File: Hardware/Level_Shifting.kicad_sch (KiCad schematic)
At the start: 49 parts, among them J11 SMA_Edge, J12 SMA_Edge, SW4 SPDT_Slide_SMD_7.2x3.5mm, U10 74LVC2T45DC, U12 74LVC2T45DC, U14 74LVC2T45DC, U15 74LVC2T45DC, U16 74LVC2T45DC, U8 74LVC2T45DC, U9 74LVC2T45DC

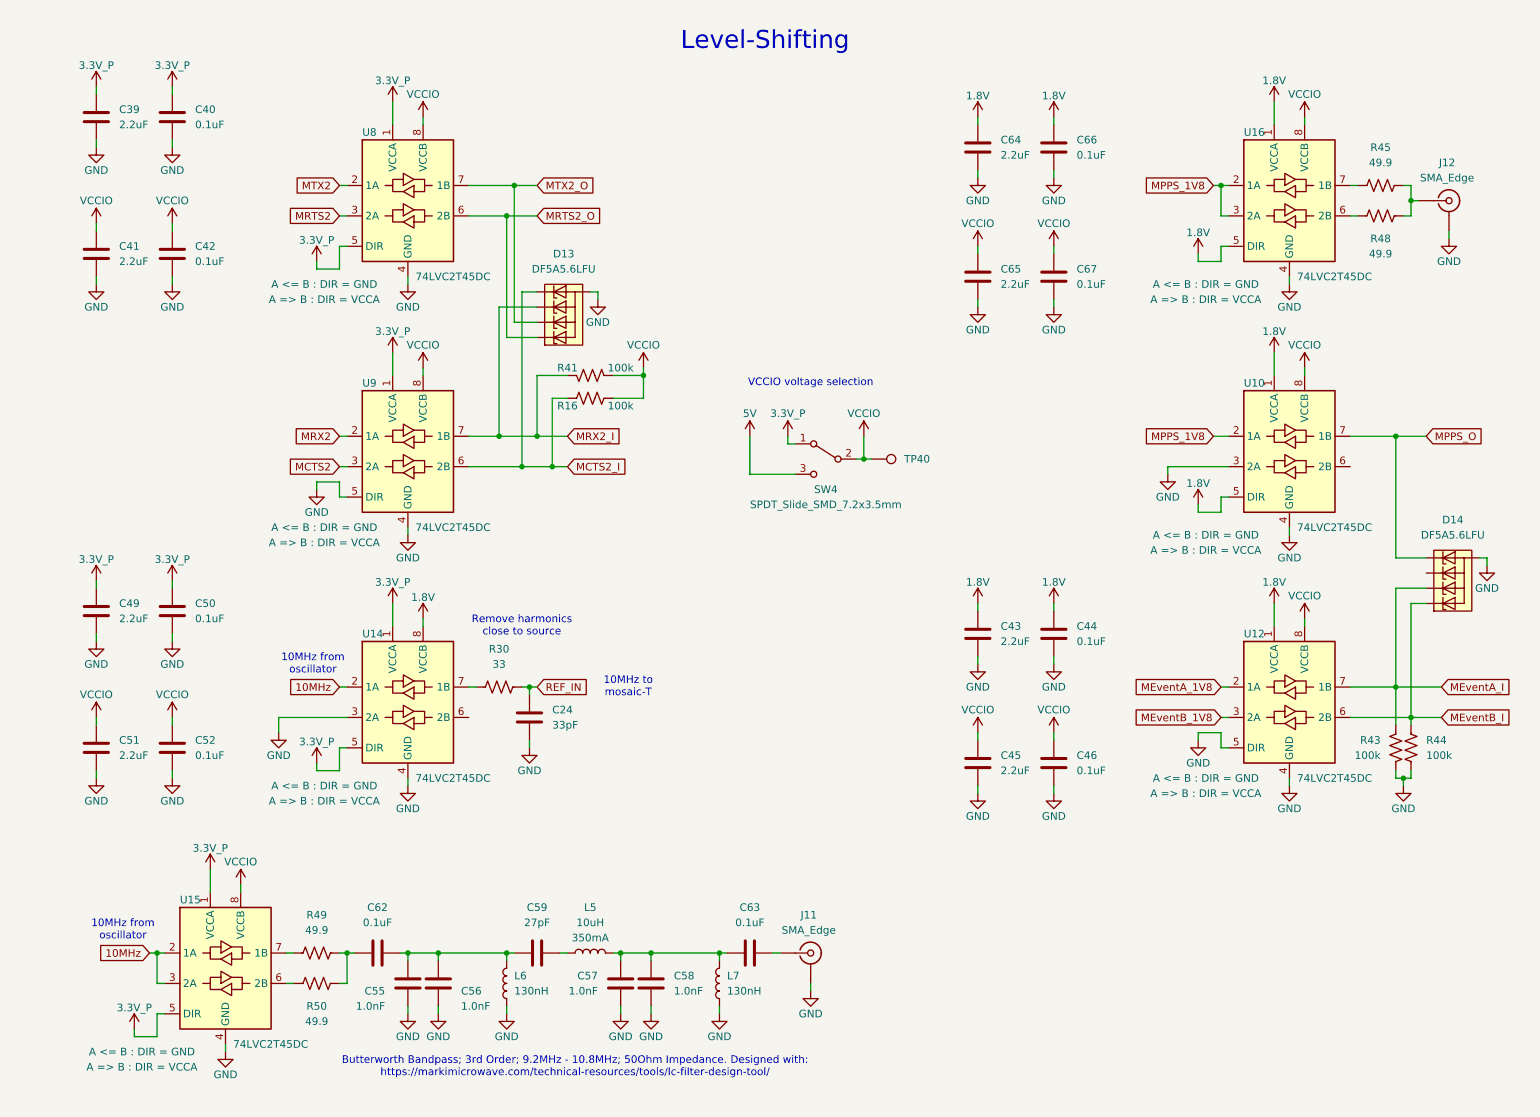
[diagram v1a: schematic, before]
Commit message: Updates for v1.0 PCB
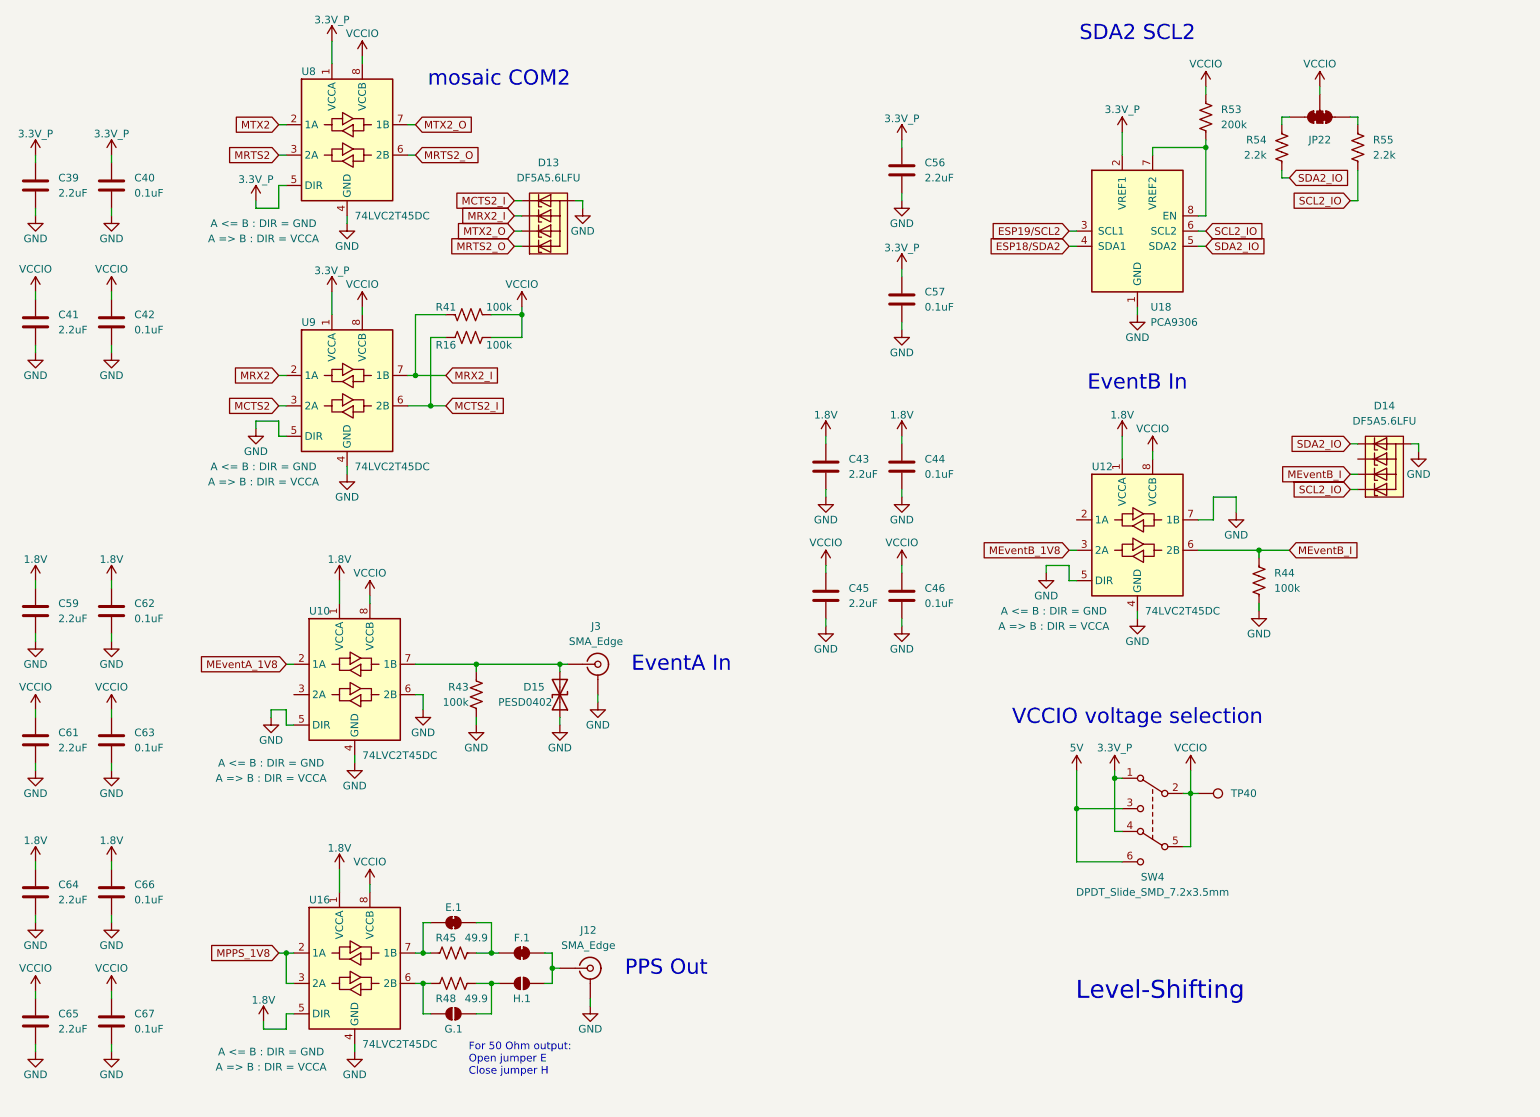
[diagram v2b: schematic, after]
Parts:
- removed C24: 33pF, SparkFun-Capacitor:C_0603_1608Metric, symbol SparkFun-Capacitor:33pF_0603_50V_5%
- removed C49, C51: 2.2uF, SparkFun-Capacitor:C_0603_1608Metric, symbol SparkFun-Capacitor:2.2uF_0603_10V_20%
- removed C50, C52: 0.1uF, SparkFun-Capacitor:C_0603_1608Metric, symbol SparkFun-Capacitor:0.1uF_0603_25V_20%
- removed C55, C56, C57, C58: 1.0nF, SparkFun-Capacitor:C_0603_1608Metric, symbol SparkFun-Capacitor:1.0nF_0603_50V_10%
- removed C59: 27pF, SparkFun-Capacitor:C_0603_1608Metric, symbol SparkFun-Capacitor:27pF_0603_50V_5%
- removed J11: SMA_Edge, SparkFun-Connector:SMA_Edge, symbol SparkFun-RF:SMA_EdgeMount
- removed L5: 10uH, SparkFun-Capacitor:C_0805_2012Metric, symbol SparkFun-Coil:10uH_0805_0.35A
- removed L6, L7: 130nH, SparkFun-Capacitor:C_0603_1608Metric, symbol SparkFun-Coil:130nH_0603_170mA
- removed R30: 33, SparkFun-Resistor:R_0603_1608Metric, symbol SparkFun-Resistor:33_0603
- removed R49, R50: 49.9, SparkFun-Resistor:R_0603_1608Metric, symbol SparkFun-Resistor:49.9_0603
- removed SW4: SPDT_Slide_SMD_7.2x3.5mm, SparkFun-Switch:Slide_DPDT_SMD_7.2x3.5mm, symbol SparkFun-Switch:SPDT_Slide_SMD_7.2x3.5mm
- removed U14, U15: 74LVC2T45DC, SparkFun-Semiconductor-Standard:VSSOP8_SOT765-1, symbol SparkFun-IC-Logic:74LVC2T45DC
- added C56, C59, C61: 2.2uF, SparkFun-Capacitor:C_0603_1608Metric, symbol SparkFun-Capacitor:2.2uF_0603_10V_20%
- added C57: 0.1uF, SparkFun-Capacitor:C_0603_1608Metric, symbol SparkFun-Capacitor:0.1uF_0603_25V_20%
- added D15: PESD0402, SparkFun-Capacitor:C_0402_1005Metric, symbol SparkFun-DiscreteSemi:D_TVS_0402
- added E.1, F.1: ~, SparkFun-Jumper:Jumper_2_NC_Trace, symbol SparkFun-Jumper:SolderJumper_2_Bridged
- added G.1, H.1: ~, SparkFun-Jumper:Jumper_2_NO, symbol SparkFun-Jumper:SolderJumper_2_Open
- added J3: SMA_Edge, SparkFun-Connector:SMA_Edge, symbol SparkFun-RF:SMA_EdgeMount
- added JP22: ~, SparkFun-Jumper:Jumper_3_NC-2_Trace, symbol SparkFun-Jumper:SolderJumper_3_Bridged123
- added R53: 200k, SparkFun-Resistor:R_0603_1608Metric, symbol SparkFun-Resistor:200k_0603
- added R54, R55: 2.2k, SparkFun-Resistor:R_0603_1608Metric, symbol SparkFun-Resistor:2.2k_0603
- added SW4: DPDT_Slide_SMD_7.2x3.5mm, SparkFun-Switch:Slide_DPDT_SMD_7.2x3.5mm, symbol SparkFun-Switch:DPDT_Slide_SMD_7.2x3.5mm
- added U18: PCA9306, SparkFun-Semiconductor-Standard:VSSOP8_SOT765-1, symbol SparkFun-IC-Special-Function:PCA9306
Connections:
- net 1.8V: now also C62.1, C59.1; no longer U10.5 (DIR)
- net 3.3V_P: now also C56.1, C57.1, SW4.1 (A), SW4.4 (A), U18.2 (VREF1)
- net 5V: now also SW4.3 (C), SW4.6 (C)
- net GND: now also C62.2, C63.2, U10.5 (DIR), U10.6 (2B), U12.7 (1B), C56.2, C57.2, C59.2, C61.2, D15.1 (A1), J3.2 (Ext), U18.1 (GND); no longer U10.3 (2A)
- net MEventA_1V8: now also U10.2 (1A); no longer U12.2 (1A)
- net MEventB_I: now also D14.3 (K2); no longer D14.1 (K1)
- net MPPS_1V8: no longer U10.2 (1A)
- net VCCIO: now also C63.1, C61.1, JP22.2 (C), R53.2, SW4.2 (B), SW4.5 (B)
- net at R45.2, U16.7 (1B): now also E.1.1 (A)
- net at R48.2, U16.6 (2B): now also G.1.1 (A)
- removed net MEventA_I: D14.3 (K2), R43.1, U12.7 (1B)
- net MPPS_O: no longer names the net of U10.7 (1B)
- net MPPS_O: now also R43.1, D15.2 (A2), J3.1 (In); no longer D14.5 (K4)
- new net: F.1.2 (B), H.1.2 (B), J12.1 (In)
- new net: E.1.2 (B), F.1.1 (A), R45.1
- new net: G.1.2 (B), H.1.1 (A), R48.1
- new net: JP22.1 (A), R55.2
- new net: R53.1, U18.7 (VREF2), U18.8 (EN)
- new net: JP22.3 (B), R54.2
- new net ESP18/SDA2: U18.4 (SDA1)
- new net ESP19/SCL2: U18.3 (SCL1)
- new net SCL2_IO: D14.1 (K1), R55.1, U18.6 (SCL2)
- new net SDA2_IO: D14.5 (K4), R54.1, U18.5 (SDA2)
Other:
- note added: "EventA In"
- note added: "EventB In"
- note added: "For 50 Ohm output: Open jumper E Close jumper H"
- note added: "PPS Out"
- note added: "SDA2 SCL2"
- note added: "mosaic COM2"
- note removed: "10MHz from oscillator"
- note removed: "10MHz to mosaic-T"
- note removed: "Butterworth Bandpass; 3rd Order; 9.2MHz - 10.8MHz; 50Ohm Impedance. Designed with: https://markimicrowave.com/technical-resources/tools/lc-filter-design-tool/"
- note removed: "Remove harmonics close to source"
- title: (none) -> Level Shifting
- moved on the sheet: C39, C40, C41, C42, C43, C44, C45, C46, C64, C65, C66, C67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

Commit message: Add jumpers for 2.8V and 1.8V In / Out
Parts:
- added J.1, M.1: ~, SparkFun-Jumper:Jumper_2_NC_Trace, symbol SparkFun-Jumper:SolderJumper_2_Bridged
- added K.1, L.1, N.1, P.1: ~, SparkFun-Jumper:Jumper_2_NO, symbol SparkFun-Jumper:SolderJumper_2_Open
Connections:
- net 1.8V: now also L.1.2 (B), P.1.2 (B)
- net VCCIO: now also J.1.2 (B), M.1.2 (B); no longer C61.1, C63.1, C65.1, C67.1, U10.8 (VCCB), U16.8 (VCCB)
- new net: C65.1, C67.1, M.1.1 (A), N.1.1 (A), P.1.1 (A), U16.8 (VCCB)
- new net: C61.1, C63.1, J.1.1 (A), K.1.1 (A), L.1.1 (A), U10.8 (VCCB)
- new net 2.8V: K.1.2 (B), N.1.2 (B)
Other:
- note added: "For 2.8V input: Open jumper J Close jumper K For 1.8V input: Open jumper J Close jumper L"
- note added: "For 2.8V output: Open jumper M Close jumper N For 1.8V output: Open jumper M Close jumper P"
- moved on the sheet: C59, C61, C62, C63, C64, C65, C66, C67, D15, E.1, F.1, G.1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

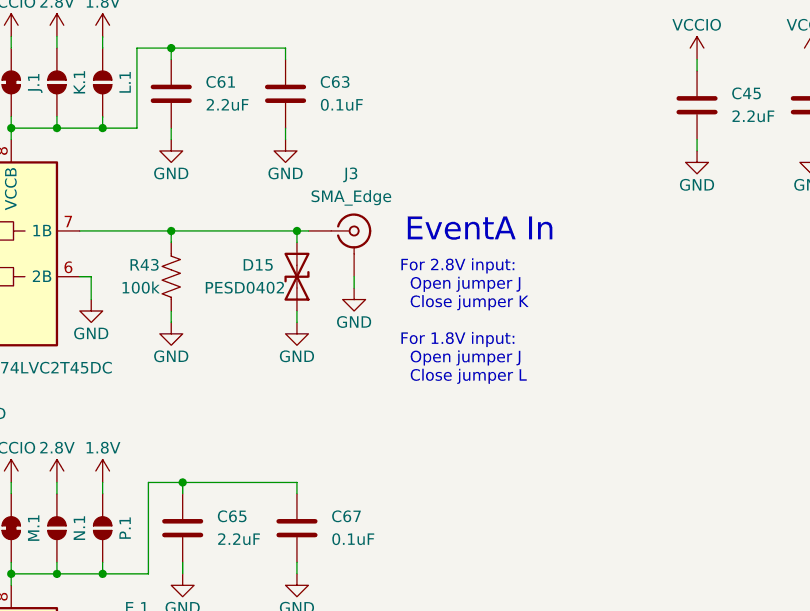
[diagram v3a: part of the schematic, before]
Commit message: Add mounting holes for SiT5811 / Rakon oscillator
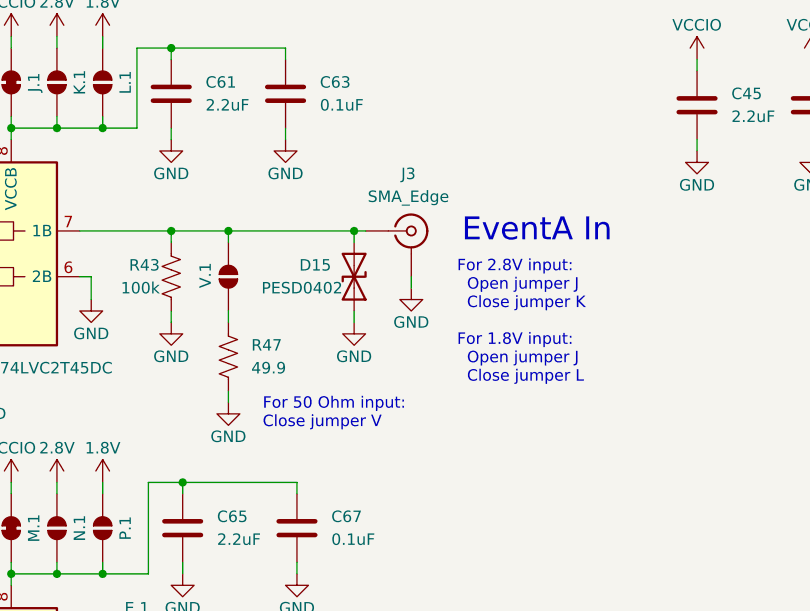
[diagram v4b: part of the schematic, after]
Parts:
- added R47: 49.9, SparkFun-Resistor:R_0603_1608Metric, symbol SparkFun-Resistor:49.9_0603
- added V.1: ~, SparkFun-Jumper:Jumper_2_NO, symbol SparkFun-Jumper:SolderJumper_2_Open
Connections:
- net GND: now also R47.1
- net at D15.2 (A2), J3.1 (In), R43.1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: now also V.1.2 (B)
- new net: R47.2, V.1.1 (A)
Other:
- note added: "For 50 Ohm input: Close jumper V"
- moved on the sheet: D15, J3

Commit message: Final changes before name change
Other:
- note added: "I/O Screw Terminal"
- note added: "I/O Screw Terminals"
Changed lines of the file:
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@@
+		)
+	)
+	(text "I/O Screw Terminals"
+		(exclude_from_sim no)
+		(at 107.95 36.83 0)
+		(effects
+			(font
+				(size 1.27 1.27)
+			)
+			(justify bottom)
 		)
 	)
@@
 		)
 	)
+	(text "I/O Screw Terminal"
+		(exclude_from_sim no)
+		(at 254 106.68 0)
+		(effects
+			(font
+				(size 1.27 1.27)
+			)
+			(justify bottom)
+		)
+	)
 	(text "Level-Shifting"
 		(exclude_from_sim no)
@@
 				(size 3 3)
 			)
+		)
+	)
+	(text "I/O Screw Terminals"
+		(exclude_from_sim no)
+		(at 240.03 54.61 0)
+		(effects
+			(font
+				(size 1.27 1.27)
+			)
+			(justify bottom)
 		)
 	)
@@
 		)
 	)
+	(text "I/O Screw Terminals"
+		(exclude_from_sim no)
+		(at 113.03 78.74 0)
+		(effects
+			(font
+				(size 1.27 1.27)
+			)
+			(justify bottom)
+		)
+	)

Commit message: Final tweaks
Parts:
- added TP48: PTH, SparkFun-Connector:1x01, symbol SparkFun-Connector:TestPoint_PTH
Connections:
- net VCCIO: now also TP48.1
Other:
- note added: "Provides VCCIO at TCXO breakouts"
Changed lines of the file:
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@@
 	(wire
 		(pts
+			(xy 242.57 146.05) (xy 243.84 146.05)
+		)
+		(stroke
+			(width 0)
+			(type default)
+		)
+	)
+	(wire
+		(pts
 			(xy 92.71 154.94) (xy 96.52 154.94)
 		)
@@
 	(wire
 		(pts
+			(xy 243.84 144.78) (xy 243.84 146.05)
+		)
+		(stroke
+			(width 0)
+			(type default)
+		)
+	)
+	(wire
+		(pts
 			(xy 236.22 27.94) (xy 236.22 29.21)
 		)
@@
 		)
 	)
+	(text "Provides VCCIO\nat TCXO breakouts"
+		(exclude_from_sim no)
+		(at 241.3 149.86 0)
+		(effects
+			(font
+				(size 1.27 1.27)
+			)
+		)
+	)
 	(text "For 50 Ohm input:\nClose jumper V"
 		(exclude_from_sim no)
@@
 	)
 	(symbol
+		(lib_id "SparkFun-PowerSymbol:VCC")
+		(at 243.84 144.78 0)
+		(unit 1)
+		(exclude_from_sim no)
+		(in_bom yes)
+		(on_board yes)
+		(dnp no)
+		(fields_autoplaced yes)
+		(property "Reference" "#PWR0265"
+			(at 243.84 148.59 0)
+			(effects
+				(font
+					(size 1.27 1.27)
+				)
+				(hide yes)
+			)
+		)
+		(property "Value" "VCCIO"
+			(at 243.84 140.97 0)
+			(do_not_autoplace yes)
+			(effects
+				(font
+					(size 1.27 1.27)
+				)
+			)
+		)
+		(property "Footprint" ""
+			(at 243.84 144.78 0)
+			(effects
+				(font
+					(size 1.27 1.27)
+				)
+				(hide yes)
+			)
+		)
+		(property "Datasheet" ""
+			(at 243.84 144.78 0)
+			(effects
+				(font
+					(size 1.27 1.27)
+				)
+				(hide yes)
+			)
+		)
+		(property "Description" "Power symbol creates a global label with name \"VCC\""
+			(at 243.84 144.78 0)
+			(effects
+				(font
+					(size 1.27 1.27)
+				)
+				(hide yes)
+			)
+		)
+		(pin "1"
+		)
+		(instances
+			(project "SparkPNT_GPSDO"
+				(path "/e3dd3ae4-244d-4cba-9cca-5d2abf83f29a/d9a77ac1-2999-4329-b708-8e6cc1b00c22"
+					(reference "#PWR0265")
+					(unit 1)
+				)
+			)
+		)
+	)
+	(symbol
 		(lib_id "power:GND")
 		(at 166.37 118.11 0)
@@
 					(unit 1)
 				)
+			)
+		)
+	)
+	(symbol
+		(lib_id "SparkFun-Connector:TestPoint_PTH")
+		(at 242.57 146.05 90)
+		(mirror x)
+		(unit 1)
+		(exclude_from_sim no)
+		(in_bom yes)
+		(on_board yes)
+		(dnp no)
+		(property "Reference" "TP48"
+			(at 234.95 146.05 90)
+			(do_not_autoplace yes)
+			(effects
+				(font
+					(size 1.27 1.27)
+				)
+			)
+		)
+		(property "Value" "PTH"
+			(at 246.38 146.05 0)
+			(effects
+				(font
+					(size 1.27 1.27)
+				)
+				(hide yes)
+			)
+		)
+		(property "Footprint" "SparkFun-Connector:1x01"
+			(at 248.92 144.78 0)
+			(effects
+				(font
+					(size 1.27 1.27)
+				)
+				(hide yes)
+			)
+		)
+		(property "Datasheet" "~"
+			(at 250.19 146.05 0)
+			(effects
+				(font
+					(size 1.27 1.27)
+				)
+				(hide yes)
+			)
+		)
+		(property "Description" "Test Point"
+			(at 242.57 146.05 0)
+			(effects
+				(font
+					(size 1.27 1.27)
+				)
+				(hide yes)
+			)
+		)
+		(pin "1"
+		)
+		(instances
+			(project "SparkPNT_GPSDO"
+				(path "/e3dd3ae4-244d-4cba-9cca-5d2abf83f29a/d9a77ac1-2999-4329-b708-8e6cc1b00c22"
+					(reference "TP48")
+					(unit 1)
+				)
